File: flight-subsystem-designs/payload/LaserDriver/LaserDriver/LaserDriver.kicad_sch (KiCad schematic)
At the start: 43 parts, among them J2 Input, J3 Laser 0, J4 Laser 1, J5 BNC, U2 MAX3967AETG+, U3 MAX3967AETG+, U4 74LVC1G04, U5 SY100ELT22ZG-TR, U7 DPC6137

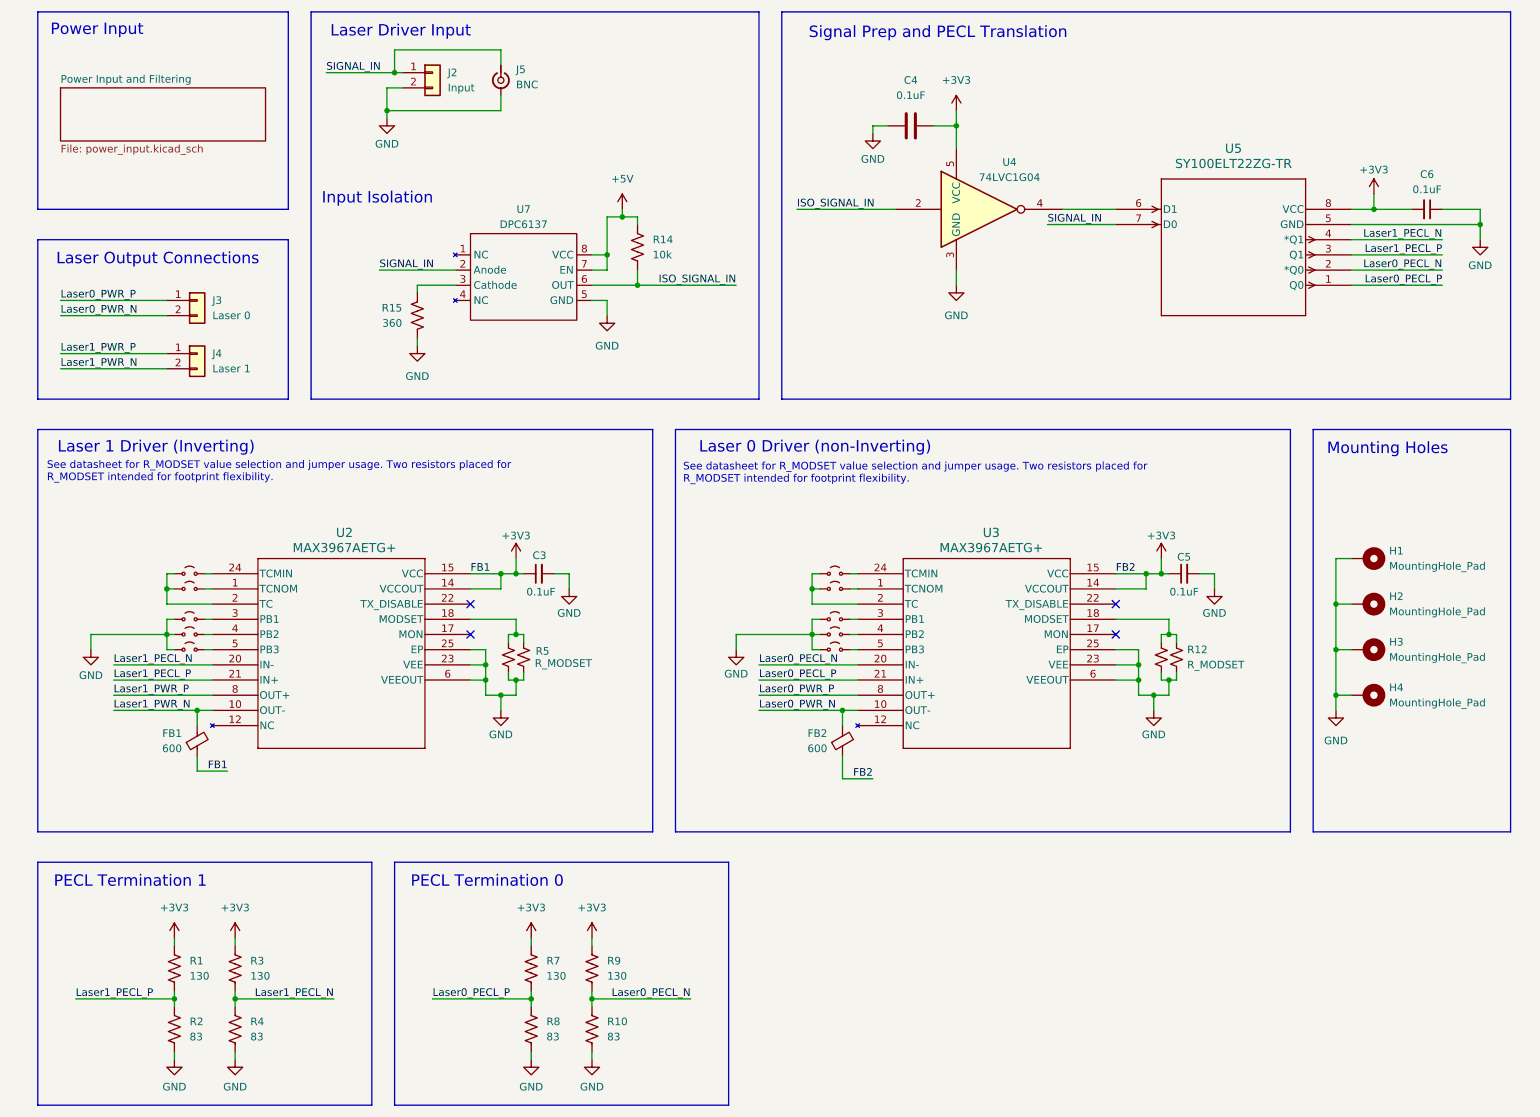
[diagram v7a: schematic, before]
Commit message: laserdriver: reset all annotations and cleared pcb :sob:
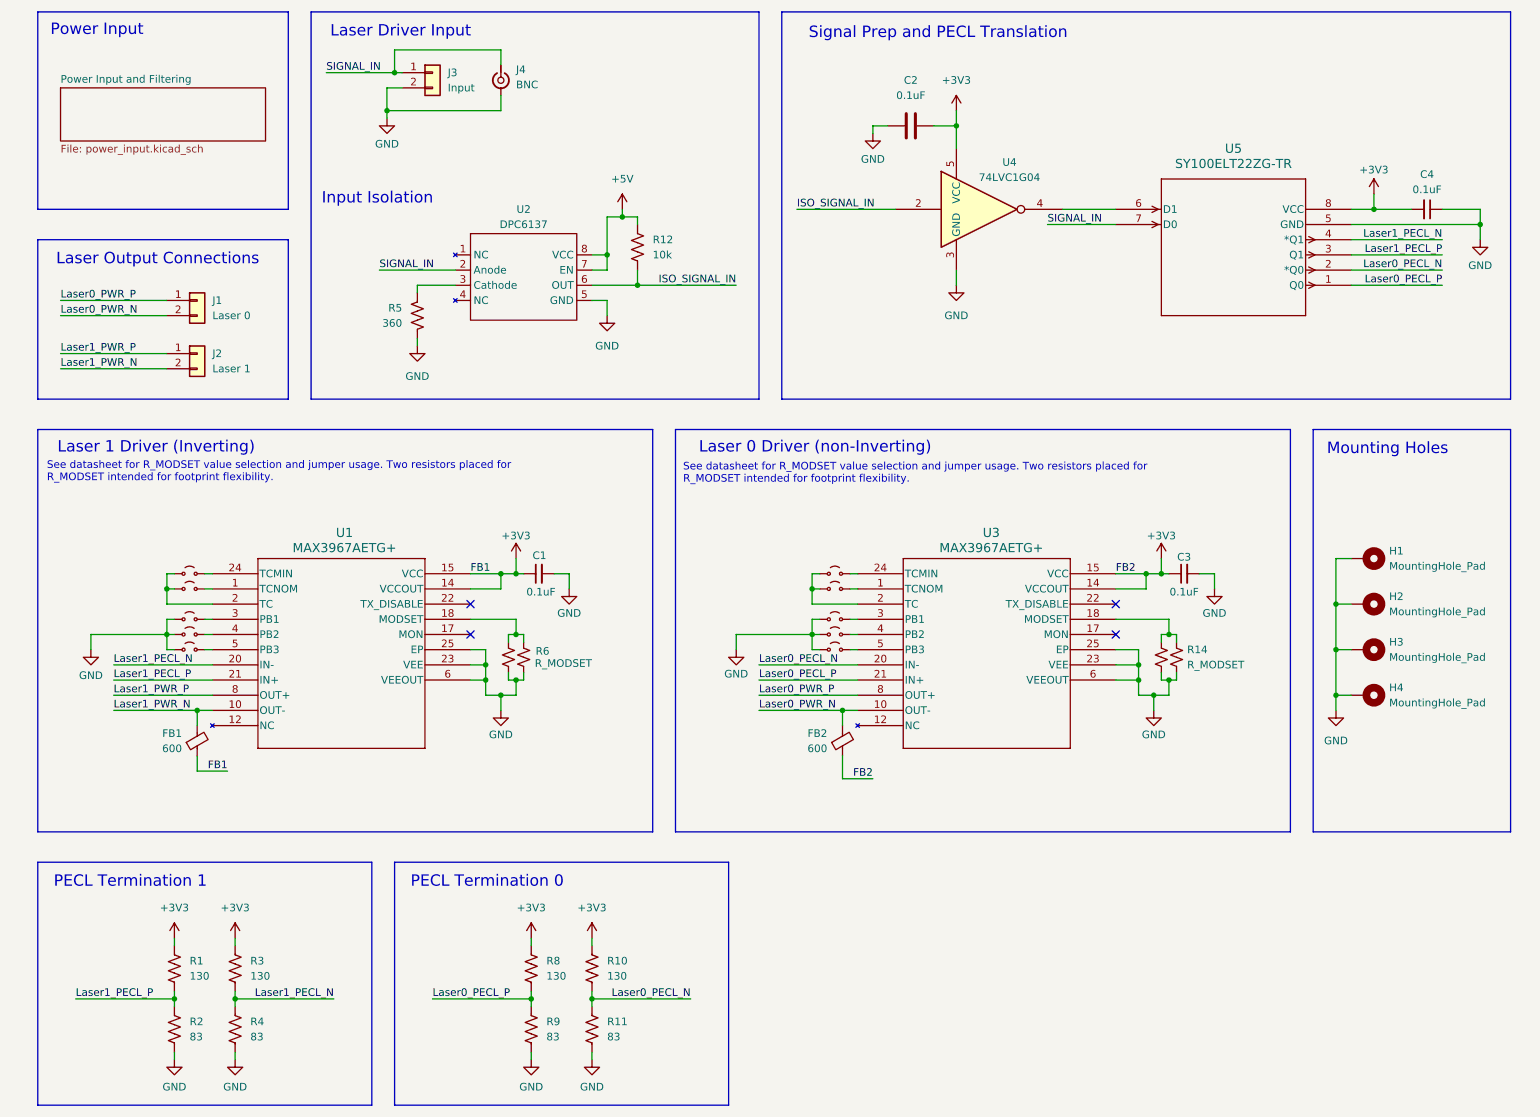
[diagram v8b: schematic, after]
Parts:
- renumbered C3 to C1, C4 to C2, C5 to C3, C6 to C4, J3 to J1, J4 to J2, J2 to J3, J5 to J4, R9 to R10, R10 to R11, R14 to R12, R11 to R13, R12 to R14, R15 to R5, R5 to R6, R6 to R7, R7 to R8, R8 to R9, U2 to U1, U7 to U2
